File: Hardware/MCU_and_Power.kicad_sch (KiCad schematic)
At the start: 3 parts, among them J1 Conn_01x20_Socket, J2 Conn_01x20_Socket

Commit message: Major Updates to Schematic
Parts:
- added C4: 10uF, symbol Device:C_Polarized
- added C5: 22uF, symbol Device:C_Polarized
- added D5: LED, symbol Device:LED
- added R13: 1K, symbol Device:R
- added U2: AMS1117-1.8, Package_TO_SOT_SMD:SOT-223-3_TabPin2, symbol Regulator_Linear:AMS1117-1.8
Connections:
- net +3V3: now also J1.1 (Pin_1), C4.1, R13.1, U2.3 (VI)
- net GND: now also J1.14 (Pin_14), J2.20 (Pin_20), C4.2, C5.2, D5.1 (K), U2.1 (GND)
- net TFT_DC: now reaches J2.10 (Pin_10)
- net TFT_CS: now reaches J2.11 (Pin_11)
- net SCK: now reaches J2.12 (Pin_12)
- net MISO: now reaches J2.13 (Pin_13)
- net SDA: now reaches J2.15 (Pin_15)
- net SCL: now reaches J2.18 (Pin_18)
- net MOSI: now reaches J2.19 (Pin_19)
- net GPIO 15: now reaches J2.5 (Pin_5)
- net GPIO 2: now reaches J2.6 (Pin_6)
- net TFT_RST: now reaches J2.9 (Pin_9)
- net GPIO 14: now reaches J1.12 (Pin_12)
- net GPIO 13: now reaches J1.15 (Pin_15)
- net GPIO 34: now reaches J1.5 (Pin_5)
- net GPIO 35: now reaches J1.6 (Pin_6)
- net SD_CS: now reaches J1.7 (Pin_7)
- new net: D5.2 (A), R13.2
- new net 1.8V: C5.1, U2.2 (VO)
- no-connect marks 2 -> 6
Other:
- note added: "Buck Converter(3.3V to 1.8V)"
- note added: "MCU"
- note added: "Power Indicator LED"
- moved on the sheet: C1, J1, J2

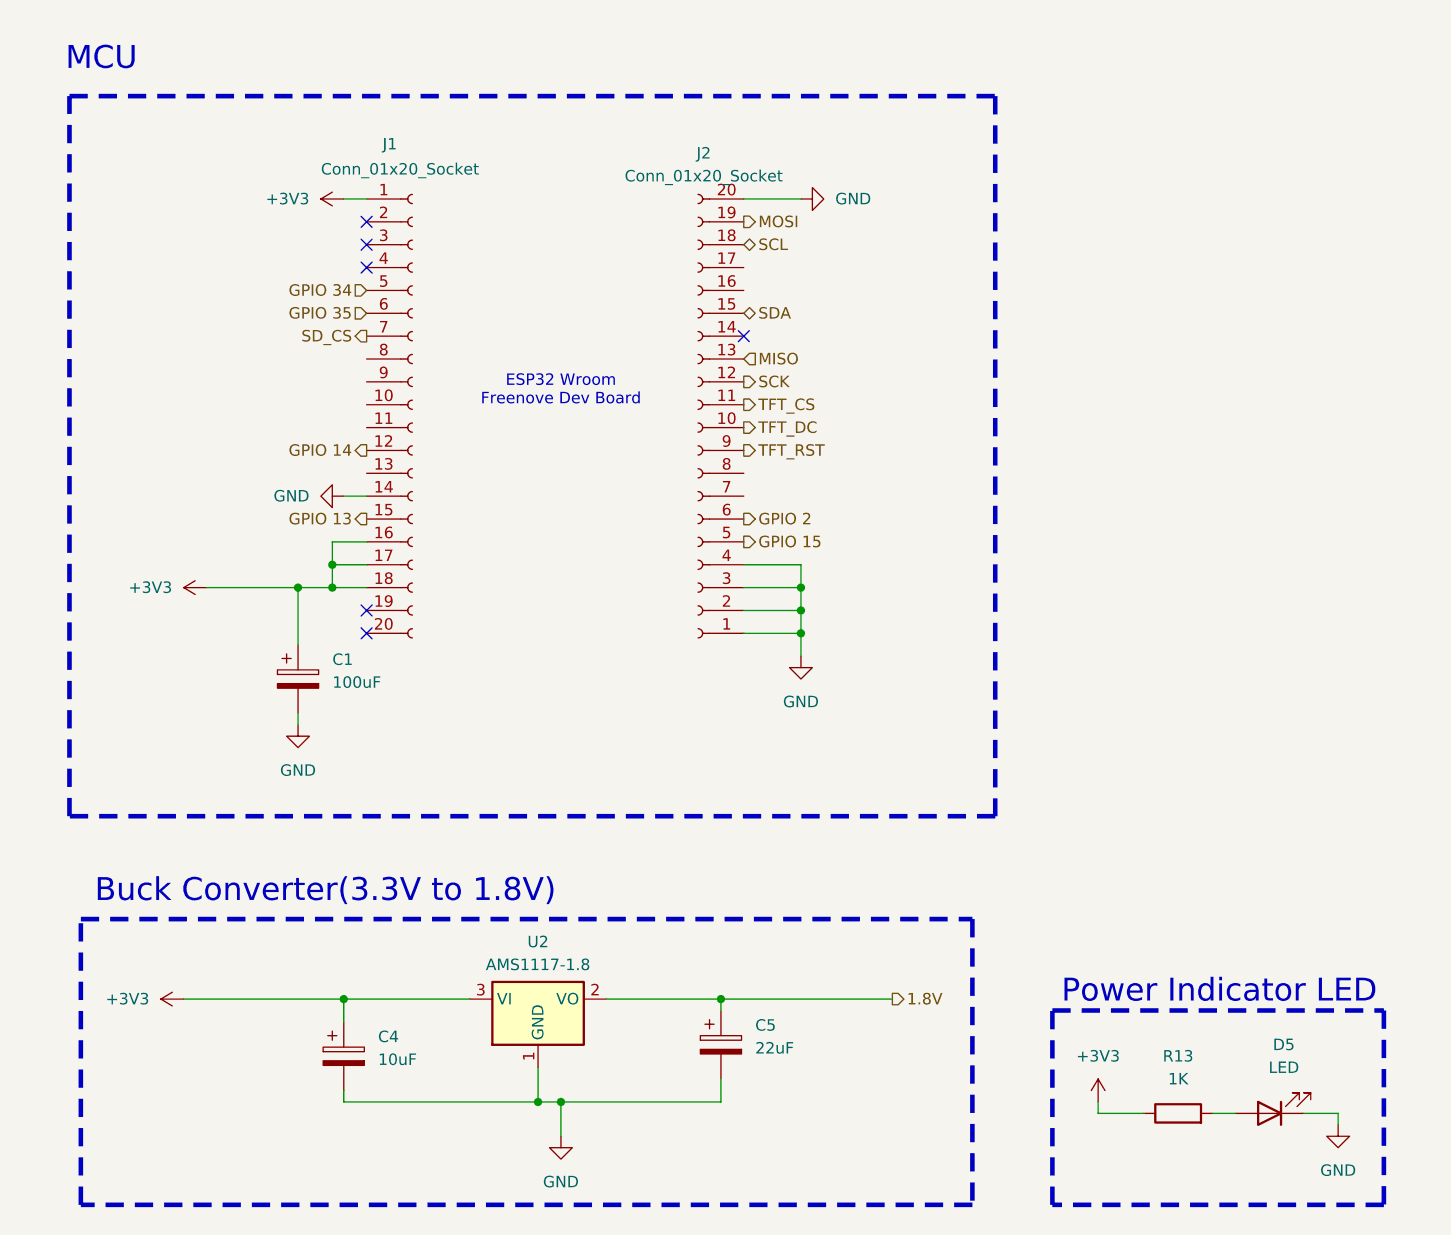
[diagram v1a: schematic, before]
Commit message: Schematic V0.9 is complete
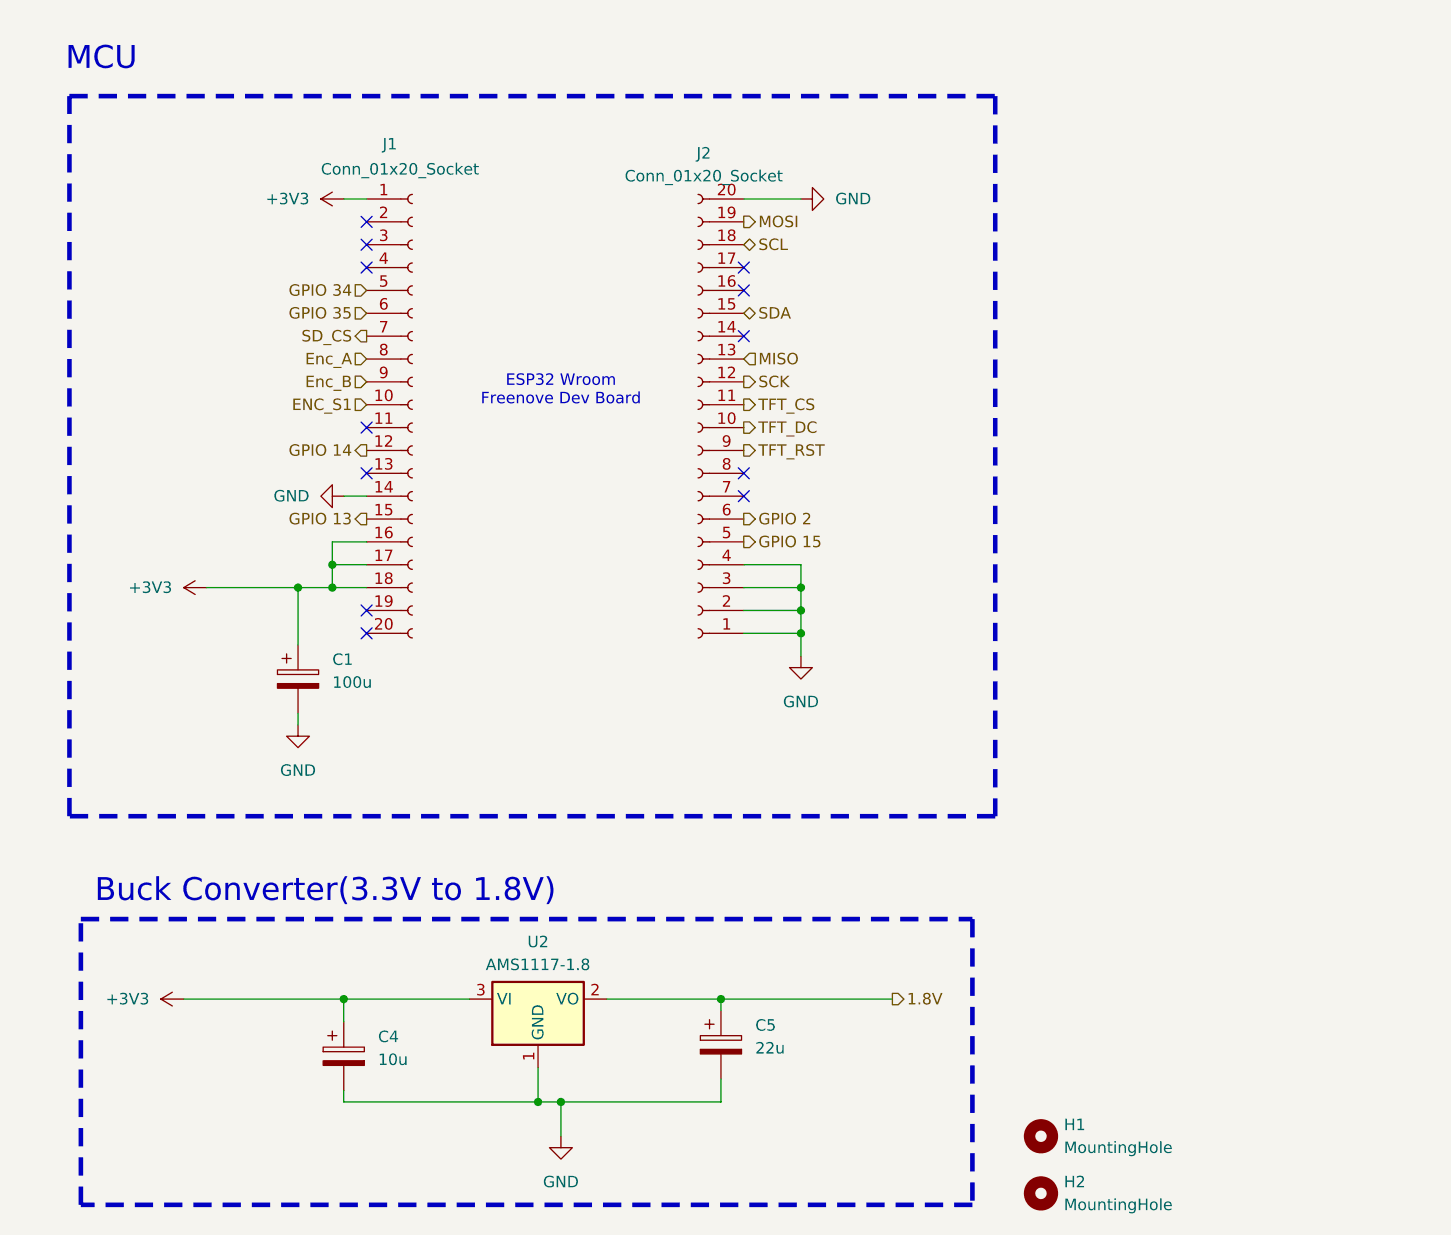
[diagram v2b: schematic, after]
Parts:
- removed D5: LED, symbol Device:LED
- removed R13: 1K, symbol Device:R
- added H1, H2: MountingHole, MountingHole:MountingHole_3.2mm_M3, symbol Mechanical:MountingHole
- C1: value 100uF -> 100u; footprint (none) -> Capacitor_THT:CP_Radial_D6.3mm_P2.50mm
- C4: value 10uF -> 10u; footprint (none) -> Capacitor_THT:CP_Radial_D5.0mm_P2.00mm
- C5: value 22uF -> 22u; footprint (none) -> Capacitor_THT:CP_Radial_D5.0mm_P2.00mm
- J1, J2: footprint (none) -> Connector_PinSocket_2.54mm:PinSocket_1x20_P2.54mm_Vertical
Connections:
- net ENC_S1: now reaches J1.10 (Pin_10)
- net Enc_A: now reaches J1.8 (Pin_8)
- net Enc_B: now reaches J1.9 (Pin_9)
- no-connect marks 6 -> 12
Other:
- note removed: "Power Indicator LED"
